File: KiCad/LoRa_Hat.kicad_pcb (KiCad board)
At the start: 2 copper layers, 65 x 56 mm, 33 parts, among them J1 GPIO, J2 OLED Display, J3 Ext, J4 Ext, J5 LoRa RF SMA, J6 PJ-036DH, J7 Conn_01x01_Female, J8 Conn_01x01_Female, SW1 SW_Push, SW2 SW_Push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

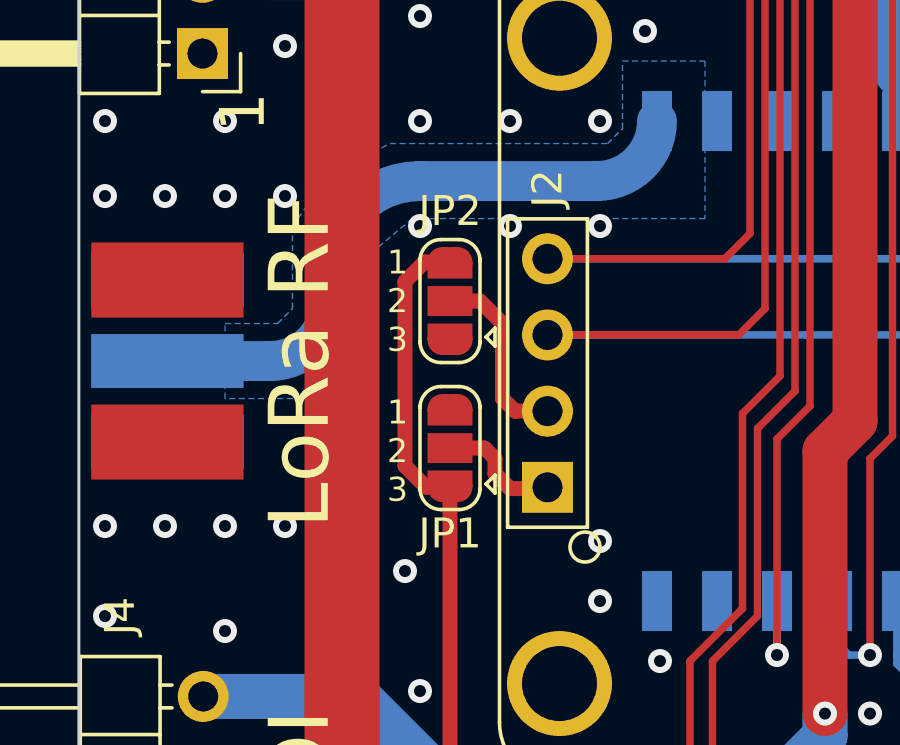
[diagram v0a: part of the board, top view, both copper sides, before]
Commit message: Schema corrections for J1 and J2 to reflect PCB silk layer print
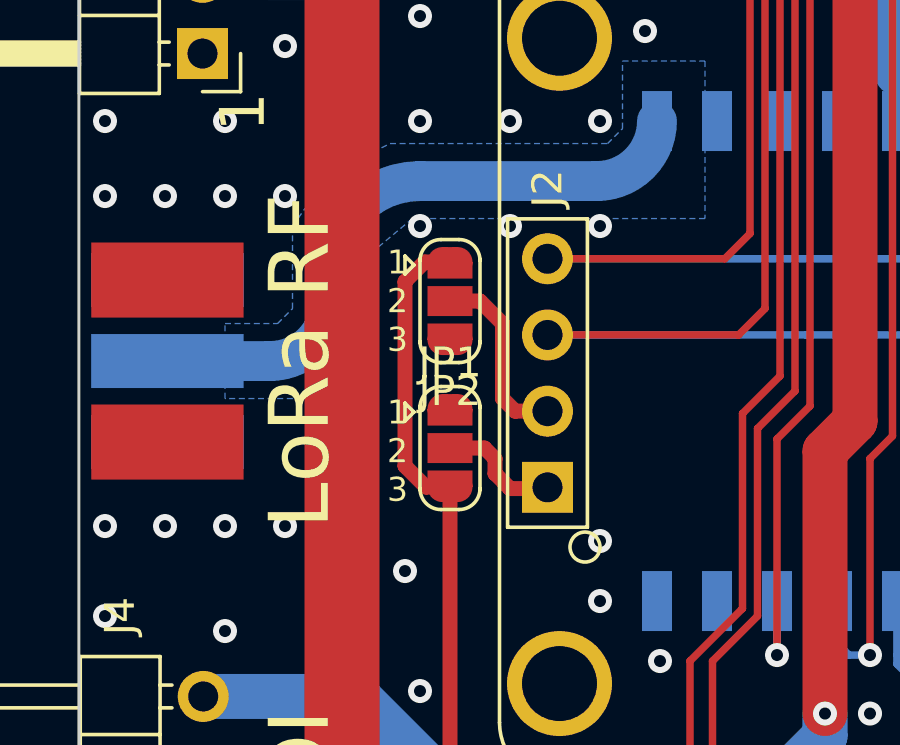
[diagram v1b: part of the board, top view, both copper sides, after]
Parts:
- turned JP1 to -90 degrees
- turned JP2 to -90 degrees
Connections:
- JP1 pad 1: +3V3 -> GND
- JP1 pad 3: GND -> +3V3
- JP2 pad 1: GND -> +3V3
- JP2 pad 3: +3V3 -> GND
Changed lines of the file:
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@@
   )
   (footprint "Jumper:SolderJumper-3_P1.3mm_Open_RoundedPad1.0x1.5mm" (layer "F.Cu")
-    (at 122.77 97.61 90)
+    (at 122.77 97.61 -90)
     (descr "SMD Solder 3-pad Jumper, 1x1.5mm rounded Pads, 0.3mm gap, open")
     (tags "solder jumper open")
@@
     (property "ki_keywords" "Jumper SPDT")
     (attr exclude_from_pos_files)
-    (fp_text reference "JP2" (at 3 0 180) (layer "F.SilkS")
+    (fp_text reference "JP2" (at 3 0) (layer "F.SilkS")
         (effects (font (size 1 1) (thickness 0.15)))
     )
@@
     (fp_line (start 2.3 1.25) (end 2.3 -1.25)
       (stroke (width 0.05) (type solid)) (layer "F.CrtYd"))
-    (pad "1" smd custom (at -1.3 0 90) (size 1 0.5) (layers "F.Cu" "F.Mask")
-      (net 6 "GND") (pinfunction "A") (pintype "passive") (zone_connect 2) (thermal_bridge_angle 45)
+    (pad "1" smd custom (at -1.3 0 270) (size 1 0.5) (layers "F.Cu" "F.Mask")
+      (net 1 "+3V3") (pinfunction "A") (pintype "passive") (zone_connect 2) (thermal_bridge_angle 45)
       (options (clearance outline) (anchor rect))
       (primitives
@@
           (width 0) (fill yes))
       ))
-    (pad "2" smd rect (at 0 0 90) (size 1 1.5) (layers "F.Cu" "F.Mask")
+    (pad "2" smd rect (at 0 0 270) (size 1 1.5) (layers "F.Cu" "F.Mask")
       (net 38 "DP2") (pinfunction "C") (pintype "passive"))
-    (pad "3" smd custom (at 1.3 0 90) (size 1 0.5) (layers "F.Cu" "F.Mask")
-      (net 1 "+3V3") (pinfunction "B") (pintype "passive") (zone_connect 2) (thermal_bridge_angle 45)
+    (pad "3" smd custom (at 1.3 0 270) (size 1 0.5) (layers "F.Cu" "F.Mask")
+      (net 6 "GND") (pinfunction "B") (pintype "passive") (zone_connect 2) (thermal_bridge_angle 45)
       (options (clearance outline) (anchor rect))
       (primitives
@@
   )
   (footprint "Jumper:SolderJumper-3_P1.3mm_Open_RoundedPad1.0x1.5mm" (layer "F.Cu")
-    (at 122.77 102.51 90)
+    (at 122.77 102.51 -90)
     (descr "SMD Solder 3-pad Jumper, 1x1.5mm rounded Pads, 0.3mm gap, open")
     (tags "solder jumper open")
@@
     (property "ki_keywords" "Jumper SPDT")
     (attr exclude_from_pos_files)
-    (fp_text reference "JP1" (at -2.85 0 180) (layer "F.SilkS")
+    (fp_text reference "JP1" (at -2.85 0) (layer "F.SilkS")
         (effects (font (size 1 1) (thickness 0.15)))
     )
@@
     (fp_line (start 2.3 1.25) (end 2.3 -1.25)
       (stroke (width 0.05) (type solid)) (layer "F.CrtYd"))
-    (pad "1" smd custom (at -1.3 0 90) (size 1 0.5) (layers "F.Cu" "F.Mask")
-      (net 1 "+3V3") (pinfunction "A") (pintype "passive") (zone_connect 2) (thermal_bridge_angle 45)
+    (pad "1" smd custom (at -1.3 0 270) (size 1 0.5) (layers "F.Cu" "F.Mask")
+      (net 6 "GND") (pinfunction "A") (pintype "passive") (zone_connect 2) (thermal_bridge_angle 45)
       (options (clearance outline) (anchor rect))
       (primitives
@@
           (width 0) (fill yes))
       ))
-    (pad "2" smd rect (at 0 0 90) (size 1 1.5) (layers "F.Cu" "F.Mask")
+    (pad "2" smd rect (at 0 0 270) (size 1 1.5) (layers "F.Cu" "F.Mask")
       (net 37 "DP1") (pinfunction "C") (pintype "passive"))
-    (pad "3" smd custom (at 1.3 0 90) (size 1 0.5) (layers "F.Cu" "F.Mask")
-      (net 6 "GND") (pinfunction "B") (pintype "passive") (zone_connect 2) (thermal_bridge_angle 45)
+    (pad "3" smd custom (at 1.3 0 270) (size 1 0.5) (layers "F.Cu" "F.Mask")
+      (net 1 "+3V3") (pinfunction "B") (pintype "passive") (zone_connect 2) (thermal_bridge_angle 45)
       (options (clearance outline) (anchor rect))
       (primitives
